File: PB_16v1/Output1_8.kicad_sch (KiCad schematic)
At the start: 20 parts, among them J1 String1, J2 String2, J3 String3, J4 String4, J5 String5, J6 String6, J7 String7, J8 String8, U3 SN74HCT245N

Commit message: fixing some of the rescue libraries
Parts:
- C3: symbol PB_16-rescue:C-Device -> Device:C
- RN1, RN2: symbol PB_16-rescue:R_Pack04_SIP-Device -> Device:R_Pack04_SIP
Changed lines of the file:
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@@
     (pin "1")
   )
-  (symbol (lib_id "PB_16-rescue:C-Device") (at 134.112 107.696 0) (unit 1)
+  (symbol (lib_id "Device:C") (at 134.112 107.696 0) (unit 1)
     (in_bom yes) (on_board yes)
     (property "Reference" "C3" (id 0) (at 137.033 106.5276 0)
@@
     (pin "1")
   )
-  (symbol (lib_id "PB_16-rescue:R_Pack04_SIP-Device") (at 208.28 129.032 0) (mirror x) (unit 1)
+  (symbol (lib_id "Device:R_Pack04_SIP") (at 208.28 129.032 0) (mirror x) (unit 1)
     (in_bom yes) (on_board yes)
     (property "Reference" "RN2" (id 0) (at 207.2132 134.239 90)
@@
     (pin "2_2")
   )
-  (symbol (lib_id "PB_16-rescue:R_Pack04_SIP-Device") (at 163.322 138.176 0) (mirror x) (unit 1)
+  (symbol (lib_id "Device:R_Pack04_SIP") (at 163.322 138.176 0) (mirror x) (unit 1)
     (in_bom yes) (on_board yes)
     (property "Reference" "RN1" (id 0) (at 162.2552 143.383 90)

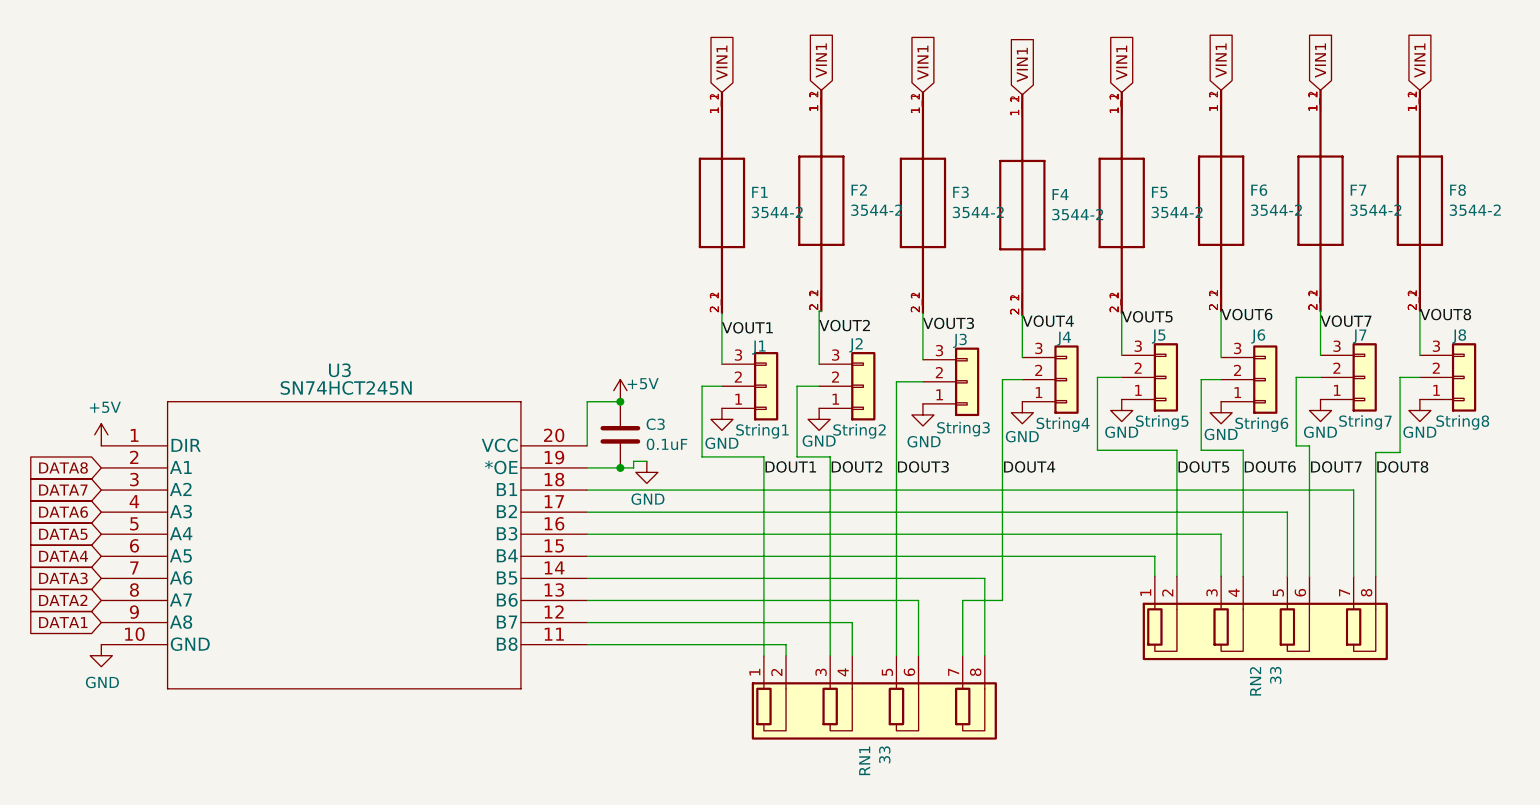
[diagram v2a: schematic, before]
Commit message: update to kicad9
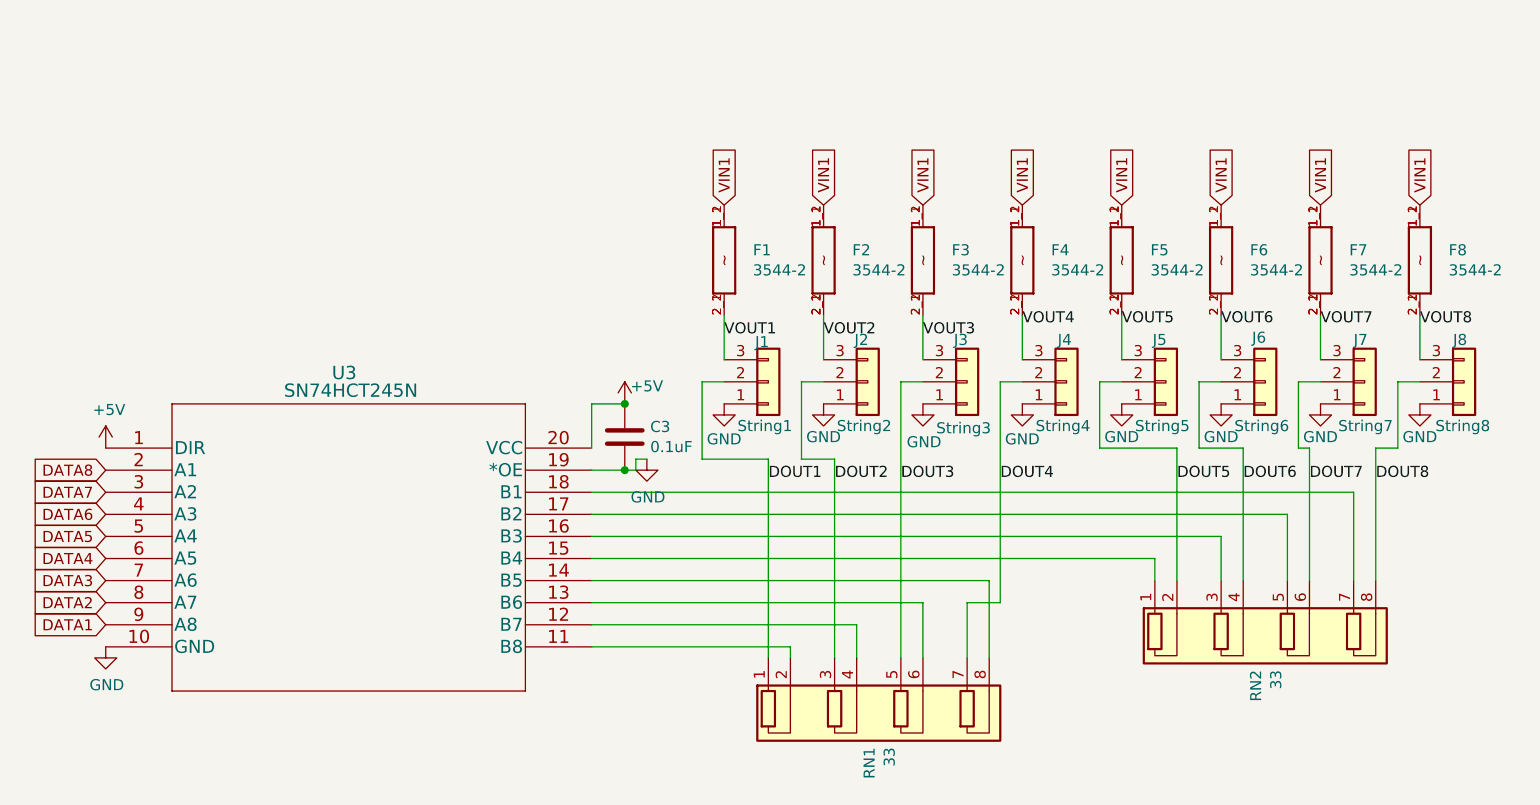
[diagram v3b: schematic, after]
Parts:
- F1, F2, F3, F4, F5, F6, F7, F8: footprint Keystone_Fuse:FUSE_3544-2 -> Scotts:FUSE_3544-2; symbol PB_16-rescue:3544-2-Keystone_Fuse -> Scotts:3544-2; LCSC (none) -> C492610
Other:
- moved on the sheet: C3, F1, F2, F3, F4, F5, F6, F7, F8, J1, J2, J5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
